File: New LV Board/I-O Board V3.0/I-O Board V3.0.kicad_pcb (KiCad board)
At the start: 2 copper layers, 58.1 x 146.2 mm, 22 parts, among them J1 PH1-10-UA, J10 691137710002, J11 691137710002, J12 20-0600-21, J12 Conn_01x15, J13 Conn_01x15, J2 *, J3 *, J4 *, J5 Conn_01x15, J6 20-0600-21, J7 691137710002, J8 691137710002, J9 691137710002

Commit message: IO Board V3.0 done?
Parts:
- removed J10, J11, J8, J9: 691137710002, I-O_Footprints:691137710002
- removed the J7 at (86.5, 27.0)
- added J16: 2604-1101, MotorSports_KICad:CONN_2604-1101_WAG, F.Cu at (120.9, 149.6)
- added J17: 2604-1101, MotorSports_KICad:CONN_2604-1101_WAG, F.Cu at (121.1, 38.4)
- added J18: 2604-1101, MotorSports_KICad:CONN_2604-1101_WAG, F.Cu at (130.8, 149.6)
- added J19: 2604-1101, MotorSports_KICad:CONN_2604-1101_WAG, F.Cu at (141.4, 149.5)
- added J20: 2604-1101, MotorSports_KICad:CONN_2604-1101_WAG, F.Cu at (142.2, 49.3)
- moved F1 45.1 mm to (134.4, 49.0), turned to 180 degrees
- moved R30 37.4 mm to (108.7, 164.7)
- moved R29 37.4 mm to (97.0, 164.7)
- moved J2 36.8 mm to (112.7, 58.1)
- moved J3 36.8 mm to (112.7, 98.4)
- moved J4 36.8 mm to (112.7, 138.9)
- moved J6 36.8 mm to (123.4, 84.4)
- moved J7 36.8 mm to (135.0, 83.9)
- moved R23 36.8 mm to (121.0, 134.9)
- moved R26 36.8 mm to (121.0, 130.8)
- moved R28 36.8 mm to (97.0, 168.4)
- moved J5 36.8 mm to (147.9, 84.4)
- moved R31 36.8 mm to (108.6, 168.4)
- moved J200 36.6 mm to (149.7, 121.1)
- moved J201 36.6 mm to (149.7, 29.6)
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- renumbered J12 to J200, J6 to J201, J12 to J6, J13 to J7
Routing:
- net Net-(J16-1_1): track 33.8 -> 206.1 mm
- net Net-(J18-1_1): track 188.3 -> 215.9 mm
- net Net-(J17-1_1): track 16.6 -> 26.0 mm
- net Net-(J4-Pad01): track 40.7 -> 42.8 mm, vias 0 -> 2
- net Net-(J4-Pad09): track 39.0 -> 41.0 mm, vias 0 -> 2
- net Net-(J4-Pad13): track 22.9 -> 24.9 mm, vias 0 -> 2
- net Net-(J4-Pad12): track 25.7 -> 27.6 mm, vias 0 -> 2
- net Net-(J4-Pad10): vias 0 -> 2
- net Net-(J4-Pad15): vias 0 -> 2
- net Net-(J4-Pad14): vias 0 -> 2
- net Net-(J4-Pad11): vias 0 -> 2
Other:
- board size 58.1 x 146.2 mm -> 58.1 x 143.4 mm

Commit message: IO Board changes
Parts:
- added J8: 2604-1101, I-O_Footprints:CONN_2604-1101_WAG, F.Cu at (141.4, 128.8)
- J4: renamed from J20; footprint MotorSports_KICad:CONN_2604-1101_WAG -> I-O_Footprints:CONN_2604-1101_WAG
- J5: renamed from J19; footprint MotorSports_KICad:CONN_2604-1101_WAG -> I-O_Footprints:CONN_2604-1101_WAG
- J6: renamed from J16; footprint MotorSports_KICad:CONN_2604-1101_WAG -> I-O_Footprints:CONN_2604-1101_WAG
- J7: renamed from J18; footprint MotorSports_KICad:CONN_2604-1101_WAG -> I-O_Footprints:CONN_2604-1101_WAG
- J9: renamed from J17; footprint MotorSports_KICad:CONN_2604-1101_WAG -> I-O_Footprints:CONN_2604-1101_WAG
- moved J4 24.9 mm to (120.7, 36.8), turned to 90 degrees
- moved J9 21.5 mm to (142.2, 34.9), turned to 0 degrees
- moved F1 15.1 mm to (120.7, 42.7), turned to 0 degrees
- moved R31 0.13 mm to (108.7, 168.4)
- renumbered J2 to J1-A1, J5 to J1-B1, J3 to J2-A1, J6 to J2-B1, J4 to J3-A1, J7 to J3-B1, J201 to PH2, J200 to PH3, REF** to PH4
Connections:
- F1 pad 1: Net-(J16-1_1) -> Net-(J3-B1-Pin_11)
- F1 pad 2: Net-(J16-1_1) -> Net-(J3-B1-Pin_11)
- J1-A1 pad S1: Net-(J18-1_1) -> Net-(J3-B1-Pin_14)
- J1-A1 pad S2: Net-(J18-1_1) -> Net-(J3-B1-Pin_14)
- J2-A1 pad S1: Net-(J18-1_1) -> Net-(J3-B1-Pin_14)
- J2-A1 pad S2: Net-(J18-1_1) -> Net-(J3-B1-Pin_14)
- J3-A1 pad S1: Net-(J18-1_1) -> Net-(J3-B1-Pin_14)
- J3-A1 pad S2: Net-(J18-1_1) -> Net-(J3-B1-Pin_14)
- J3-B1 pad 10: unconnected-(J7-Pin_10-Pad10) -> Net-(J3-B1-Pin_10)
- J3-B1 pad 11: unconnected-(J7-Pin_11-Pad11) -> Net-(J3-B1-Pin_11)
- J3-B1 pad 12: unconnected-(J7-Pin_12-Pad12) -> Net-(J3-B1-Pin_11)
- J3-B1 pad 13: unconnected-(J7-Pin_13-Pad13) -> Net-(J3-B1-Pin_11)
- J3-B1 pad 14: unconnected-(J7-Pin_14-Pad14) -> Net-(J3-B1-Pin_14)
- J3-B1 pad 15: unconnected-(J7-Pin_15-Pad15) -> Net-(J3-B1-Pin_14)
- J3-B1 pad 8: unconnected-(J7-Pin_8-Pad8) -> Net-(J3-B1-Pin_10)
- J3-B1 pad 9: unconnected-(J7-Pin_9-Pad9) -> Net-(J3-B1-Pin_10)
- J4 pad 1: Net-(J16-1_1) -> Net-(J3-B1-Pin_11)
- J4 pad 2: Net-(J16-1_1) -> Net-(J3-B1-Pin_11)
- J5 pad 1: Net-(J18-1_1) -> Net-(J3-B1-Pin_14)
- J5 pad 2: Net-(J18-1_1) -> Net-(J3-B1-Pin_14)
- J6 pad 1: Net-(J16-1_1) -> Net-(J3-B1-Pin_11)
- J6 pad 2: Net-(J16-1_1) -> Net-(J3-B1-Pin_11)
- J7 pad 1: Net-(J18-1_1) -> Net-(J3-B1-Pin_14)
- J7 pad 2: Net-(J18-1_1) -> Net-(J3-B1-Pin_14)
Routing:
- net Net-(J3-B1-Pin_14): track 0.00 -> 263.6 mm
- net Net-(J3-B1-Pin_11): track 0.00 -> 241.9 mm
- net Net-(J18-1_1): track 215.9 -> 0.00 mm
- net Net-(J16-1_1): track 206.1 -> 0.00 mm
- net Net-(J3-B1-Pin_10): track 0.00 -> 42.1 mm
- net Net-(J9-1_1): track 26.0 -> 23.4 mm

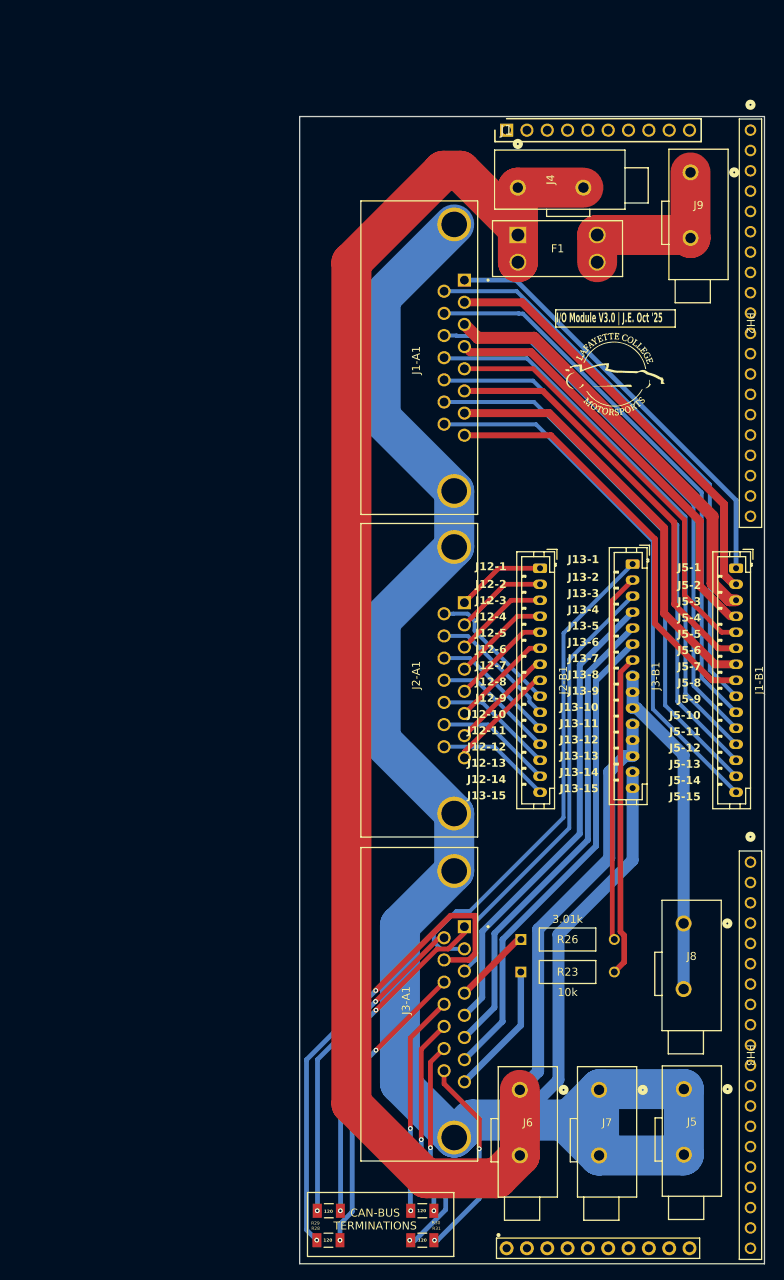
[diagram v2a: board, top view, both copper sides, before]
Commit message: Changed file name of VCU Throttle Latching to Throttle Latching Module, attempt to make VCU MPR & IMD Latch into IMD Latch & AMS Latch.
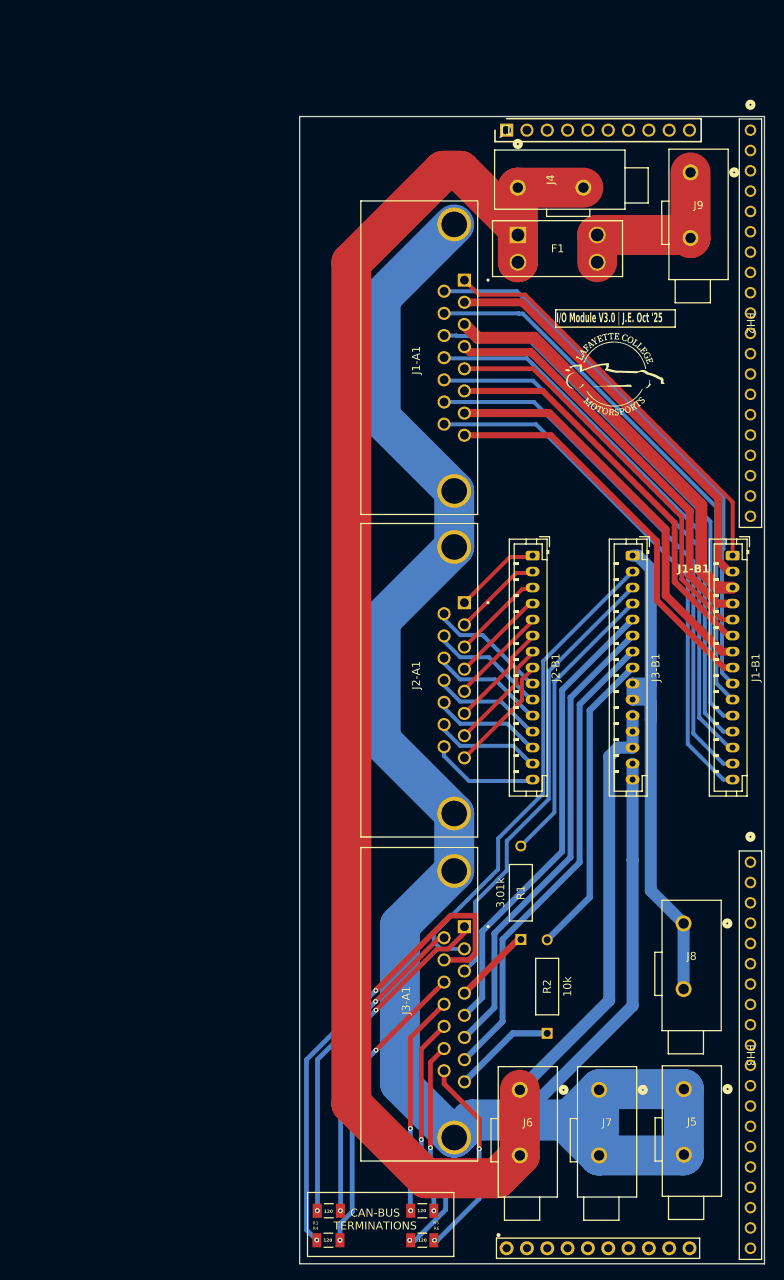
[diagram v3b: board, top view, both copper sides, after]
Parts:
- moved R2 8.34 mm to (124.3, 142.5), turned to 90 degrees
- moved J2-B1 1.84 mm to (122.5, 82.8)
- moved J1-B1 1.64 mm to (147.5, 82.8)
- moved J3-B1 1.06 mm to (135.0, 82.8)
- turned R1 to 90 degrees
- renumbered R26 to R1, R23 to R2, R29 to R3, R28 to R4, R30 to R5, R31 to R6
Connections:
- J1 pad 1: Net-(J18-1_1) -> (no net)
- J1 pad 2: Net-(J18-1_1) -> (no net)
- J1 pad 3: Net-(J18-1_1) -> (no net)
- J3-A1 pad 02: Net-(J3-B1-Pin_1) -> Net-(J3-B1-Pin_2)
- J3-A1 pad 05: Net-(J3-B1-Pin_4) -> Net-(J3-B1-Pin_5)
- J3-A1 pad 06: Net-(J3-B1-Pin_5) -> Net-(J3-B1-Pin_6)
- J3-A1 pad 07: Net-(J3-B1-Pin_6) -> Net-(J3-B1-Pin_7)
- J3-B1 pad 10: Net-(J3-B1-Pin_10) -> Net-(J3-B1-Pin_1)
- J3-B1 pad 8: Net-(J3-B1-Pin_10) -> Net-(J3-B1-Pin_8)
- J3-B1 pad 9: Net-(J3-B1-Pin_10) -> Net-(J3-B1-Pin_1)
- J8 pad 1: Net-(J3-B1-Pin_10) -> Net-(J3-B1-Pin_1)
- J8 pad 2: Net-(J3-B1-Pin_10) -> Net-(J3-B1-Pin_1)
- R1 pad 2: Net-(J3-B1-Pin_2) -> Net-(J3-B1-Pin_4)
- R2 pad 2: Net-(J3-B1-Pin_7) -> Net-(J3-B1-Pin_8)
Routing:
- net Net-(J3-B1-Pin_10): track 42.1 -> 0.00 mm
- net Net-(J3-B1-Pin_8): track 0.00 -> 38.5 mm
- net Net-(J3-B1-Pin_4): track 59.1 -> 36.1 mm
- net Net-(J3-B1-Pin_7): track 40.3 -> 59.7 mm
- net Net-(J3-B1-Pin_2): track 46.1 -> 60.8 mm
- net Net-(J3-B1-Pin_1): track 62.7 -> 68.8 mm
- net Net-(J3-A1-Pad08): track 16.7 -> 12.9 mm
- net Net-(J1-B1-Pin_8): track 52.8 -> 49.9 mm
- net Net-(J1-B1-Pin_6): track 53.3 -> 50.5 mm
- net Net-(J1-B1-Pin_7): track 53.2 -> 50.7 mm
- net Net-(J1-B1-Pin_1): track 53.9 -> 51.7 mm
- net Net-(J2-B1-Pin_10): track 16.9 -> 14.8 mm
- net Net-(J1-B1-Pin_5): track 53.1 -> 51.0 mm
- net Net-(J2-B1-Pin_9): track 17.0 -> 15.1 mm
- net Net-(J3-B1-Pin_5): track 59.9 -> 58.2 mm
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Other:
- board text added: "${REFERENCE}"
- board text added: "J1-B1"
- board text removed: "J12-1"
- board text removed: "J12-10"
- board text removed: "J12-11"
- board text removed: "J12-12"
- board text removed: "J12-13"
- board text removed: "J12-14"
- board text removed: "J12-2"
- board text removed: "J12-3"
- board text removed: "J12-4"
- board text removed: "J12-5"
- board text removed: "J12-6"
- board text removed: "J12-7"
- board text removed: "J12-8"
- board text removed: "J12-9"
- board text removed: "J13-1"
- board text removed: "J13-10"
- board text removed: "J13-11"
- board text removed: "J13-12"
- board text removed: "J13-13"
- board text removed: "J13-14"
- board text removed: "J13-15"
- board text removed: "J13-2"
- board text removed: "J13-3"
- board text removed: "J13-4"
- board text removed: "J13-5"
- board text removed: "J13-6"
- board text removed: "J13-7"
- board text removed: "J13-8"
- board text removed: "J13-9"
- board text removed: "J5-1"
- board text removed: "J5-10"
- board text removed: "J5-11"
- board text removed: "J5-12"
- board text removed: "J5-13"
- board text removed: "J5-14"
- board text removed: "J5-15"
- board text removed: "J5-2"
- board text removed: "J5-3"
- board text removed: "J5-4"
- board text removed: "J5-5"
- board text removed: "J5-6"
- board text removed: "J5-7"
- board text removed: "J5-8"
- board text removed: "J5-9"

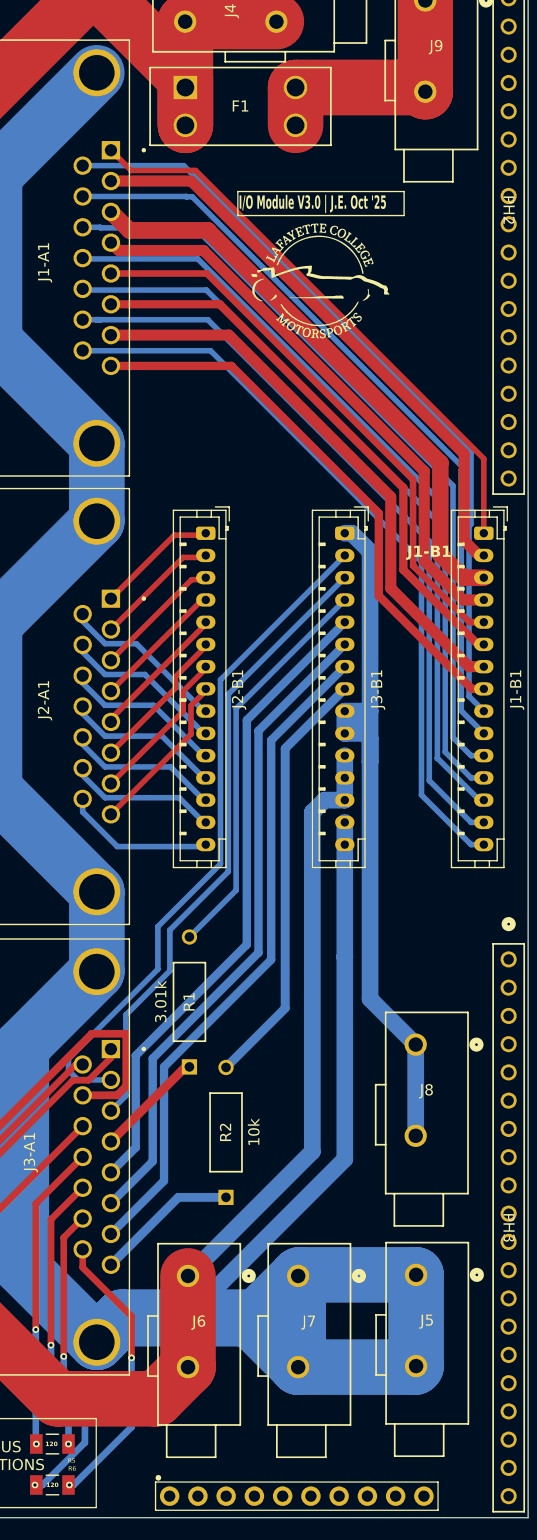
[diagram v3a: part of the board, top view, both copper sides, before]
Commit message: IO board now how 3d Models
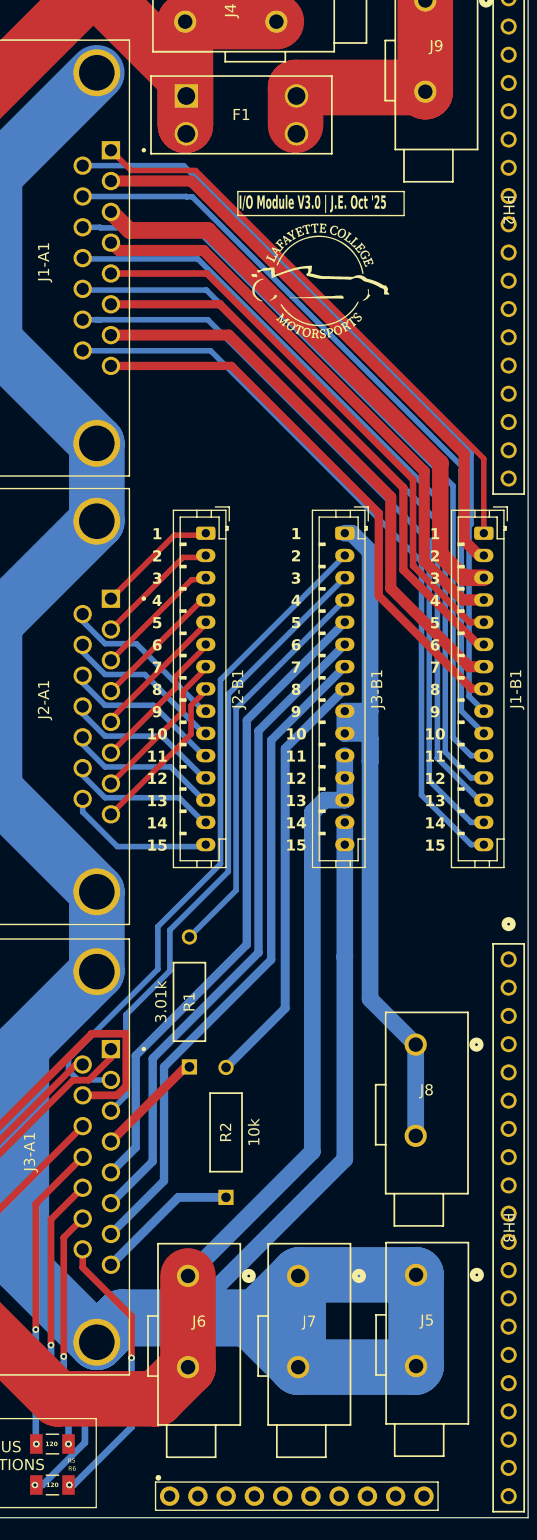
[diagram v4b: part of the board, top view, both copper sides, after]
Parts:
- moved F1 0.77 mm to (120.8, 43.5)
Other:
- board text added: "1"
- board text added: "10"
- board text added: "11"
- board text added: "12"
- board text added: "13"
- board text added: "14"
- board text added: "15"
- board text added: "2"
- board text added: "3"
- board text added: "4"
- board text added: "5"
- board text added: "6"
- board text added: "7"
- board text added: "8"
- board text added: "9"
- board text removed: "J1-B1"
